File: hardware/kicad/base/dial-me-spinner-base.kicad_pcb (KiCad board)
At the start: 2 copper layers, 57.6 x 46 mm, 23 parts, among them J1 TYPE-C-31-M-12, J2 BATT, J3 LINK, Q1 BSS138DW, SW1 TS-1187A, U1 BQ25180YBGR, U2 USBLC6-2SC6

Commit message: WIP: firmware/bring-up docs review fixes; routing in progress
Co-Authored-By: Claude Opus 5.5 <noreply@anthropic.com>
Claude-Session: https://claude.ai/code/session_01P3cqdBhxLcWY3sGUVf9LAJ
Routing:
- net GND: track 0.00 -> 175.6 mm
- net VBUS: track 0.00 -> 81.7 mm, vias 0 -> 4
- net /Base board/USB_DM: track 6.35 -> 58.4 mm, vias 0 -> 4
- net /Base board/USB_DP: track 4.35 -> 53.6 mm, vias 2 -> 4
- net VBAT: track 0.00 -> 43.5 mm, vias 0 -> 4
- net /Base board/I2C_SCL: track 0.00 -> 42.1 mm, vias 0 -> 2
- net /Base board/I2C_SDA: track 0.00 -> 35.3 mm, vias 0 -> 2
- net /Base board/BTN_N: track 0.00 -> 30.3 mm, vias 0 -> 2
- net /Base board/CHG_TSMR: track 0.00 -> 23.3 mm
- net /Base board/CHG_INT_N: track 0.00 -> 15.0 mm, vias 0 -> 1
- net /Base board/SW_GATE: track 0.00 -> 9.14 mm
- net VSYS: track 0.00 -> 8.18 mm
- net /Base board/SW_HI: track 0.00 -> 7.97 mm
- net /Base board/USB_CC1: track 0.00 -> 4.07 mm
- net /Base board/USB_CC2: track 0.00 -> 2.43 mm

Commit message: WIP: BGA escape pre-route for the charger; routing in progress
Co-Authored-By: Claude Opus 5.5 <noreply@anthropic.com>
Claude-Session: https://claude.ai/code/session_01P3cqdBhxLcWY3sGUVf9LAJ
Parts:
- moved C2 4.99 mm to (113.1, 105.8)
- moved TP2 4.29 mm to (107.6, 106.6)
- moved C1 3.08 mm to (110.2, 103.4), turned to 0 degrees
- moved C3 0.40 mm to (111.5, 108.5)
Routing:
- net /Base board/CHG_INT_N: track 15.0 -> 45.2 mm, vias 1 -> 2
- net GND: track 175.6 -> 147.9 mm
- net VBUS: track 81.7 -> 59.4 mm, vias 4 -> 0
- net /Base board/CHG_TSMR: track 23.3 -> 39.2 mm
- net VBAT: track 43.5 -> 54.4 mm, vias 4 -> 3
- net /Base board/SW_GATE: track 9.14 -> 19.4 mm, vias 0 -> 2
- net /Base board/I2C_SCL: track 42.1 -> 47.3 mm
- net /Base board/I2C_SDA: track 35.3 -> 36.5 mm
- net /Base board/USB_CC1: track 4.07 -> 5.19 mm, vias 0 -> 2
- net /Base board/USB_DM: track 58.4 -> 59.3 mm
- net VSYS: track 8.18 -> 7.38 mm
- net /Base board/USB_DP: track 53.6 -> 53.0 mm

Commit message: WIP: VSYS escape via on the charger BGA
Co-Authored-By: Claude Opus 5.5 <noreply@anthropic.com>
Claude-Session: https://claude.ai/code/session_01P3cqdBhxLcWY3sGUVf9LAJ
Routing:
- net /Base board/I2C_SCL: track 47.3 -> 41.3 mm
- net VBAT: track 54.4 -> 49.8 mm
- net /Base board/USB_DP: track 53.0 -> 51.4 mm
- net /Base board/CHG_INT_N: track 45.2 -> 44.2 mm
- net /Base board/USB_CC1: track 5.19 -> 4.44 mm
- net /Base board/USB_CC2: track 2.43 -> 3.08 mm
- net VBUS: track 59.4 -> 60.1 mm
- net /Base board/USB_DM: track 59.3 -> 58.7 mm

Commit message: Apply schematic review fixes; base board routes to 100% with zero DRC errors
- OLED VCC input disconnect is now a TPS22917 load switch (CT to VIN) instead
  of an AO3401A/2N7002 with no real inrush control
- TPD4E05U06 TVS on the TMAG5273 lines (floating 316L ring passes 2.4 mm away)
- piezo: 470R series + 1M bleed; LED_DIN pull-down moved to the shifter input
- base: explicit 2x4 DSBGA fan-out for the BQ25180, 0.4 mm power tracks,
  BAT+/GND silkscreen at the battery connector, JEITA NTC over the pack
- SPEC: side-entry link headers on both boards, 28 AWG power leads

Co-Authored-By: Claude Opus 5.5 <noreply@anthropic.com>
Claude-Session: https://claude.ai/code/session_01P3cqdBhxLcWY3sGUVf9LAJ
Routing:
- net VSYS: track 7.38 -> 39.0 mm, vias 0 -> 2
- net /Base board/CHG_INT_N: track 44.2 -> 32.3 mm, vias 2 -> 0
- net VBAT: track 49.8 -> 39.0 mm, vias 3 -> 2
- net /Base board/I2C_SCL: track 41.3 -> 30.6 mm, vias 2 -> 0
- net GND: track 148.0 -> 155.3 mm, vias 0 -> 4
- net /Base board/USB_DM: track 58.7 -> 52.8 mm, vias 4 -> 3
- net /Base board/SW_GATE: track 19.4 -> 13.7 mm, vias 2 -> 0
- net VBUS: track 60.1 -> 64.9 mm, vias 0 -> 2
- net /Base board/CHG_TSMR: track 39.3 -> 35.3 mm, vias 0 -> 3
- net /Base board/BTN_N: track 30.1 -> 27.8 mm
- net /Base board/I2C_SDA: track 36.5 -> 38.4 mm
- net /Base board/USB_DP: track 51.4 -> 50.7 mm
- net /Base board/USB_CC1: track 4.44 -> 5.09 mm
- net /Base board/USB_CC2: track 3.08 -> 2.43 mm
- added copper zone on B.Cu, net GND
- added copper zone on F.Cu, net GND

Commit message: WIP: re-placed boards (routing in progress)
Co-Authored-By: Claude Opus 5.5 <noreply@anthropic.com>
Claude-Session: https://claude.ai/code/session_01P3cqdBhxLcWY3sGUVf9LAJ
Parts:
- RT1: moved to B.Cu
- moved RT1 16.5 mm to (92.5, 102.7)
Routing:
- net GND: track 155.3 -> 0.95 mm, vias 4 -> 1
- net VBUS: track 64.9 -> 0.80 mm, vias 2 -> 0
- net /Base board/USB_DM: track 52.8 -> 6.35 mm, vias 3 -> 0
- net /Base board/USB_DP: track 50.7 -> 4.35 mm, vias 4 -> 2
- net VBAT: track 39.0 -> 1.34 mm, vias 2 -> 0
- net VSYS: track 39.0 -> 1.40 mm, vias 2 -> 0
- net /Base board/I2C_SDA: track 38.4 -> 0.80 mm, vias 2 -> 0
- net /Base board/CHG_TSMR: track 35.3 -> 0.80 mm, vias 3 -> 0
- net /Base board/CHG_INT_N: track 32.3 -> 0.80 mm
- net /Base board/I2C_SCL: track 30.6 -> 0.80 mm
- net /Base board/BTN_N: track 27.8 -> 0.00 mm, vias 2 -> 0
- net /Base board/SW_GATE: track 13.7 -> 0.00 mm
- net /Base board/SW_HI: track 8.30 -> 0.00 mm
- net /Base board/USB_CC1: track 5.09 -> 0.00 mm, vias 2 -> 0
- net /Base board/USB_CC2: track 2.43 -> 0.00 mm
- removed copper zone on B.Cu, net GND
- removed copper zone on F.Cu, net GND
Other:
- board text added: "BAT+"
- board text added: "GND"

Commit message: WIP: base board rerouted
Co-Authored-By: Claude Opus 5.5 <noreply@anthropic.com>
Claude-Session: https://claude.ai/code/session_01P3cqdBhxLcWY3sGUVf9LAJ
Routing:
- net GND: track 0.95 -> 151.5 mm, vias 1 -> 3
- net VBUS: track 0.80 -> 75.8 mm, vias 0 -> 3
- net /Base board/USB_DM: track 6.35 -> 73.6 mm, vias 0 -> 3
- net /Base board/I2C_SDA: track 0.80 -> 60.7 mm, vias 0 -> 4
- net /Base board/USB_DP: track 4.35 -> 57.7 mm, vias 2 -> 4
- net VBAT: track 1.34 -> 46.1 mm
- net /Base board/CHG_INT_N: track 0.80 -> 42.7 mm, vias 0 -> 2
- net /Base board/BTN_N: track 0.00 -> 40.9 mm, vias 0 -> 2
- net /Base board/I2C_SCL: track 0.80 -> 37.2 mm, vias 0 -> 2
- net VSYS: track 1.40 -> 36.0 mm, vias 0 -> 2
- net /Base board/CHG_TSMR: track 0.80 -> 23.0 mm, vias 0 -> 2
- net /Base board/SW_GATE: track 0.00 -> 13.2 mm
- net /Base board/USB_CC1: track 0.00 -> 9.80 mm
- net /Base board/SW_HI: track 0.00 -> 7.85 mm
- net /Base board/USB_CC2: track 0.00 -> 5.09 mm, vias 0 -> 2
- added copper zone on B.Cu, net GND
- added copper zone on F.Cu, net GND

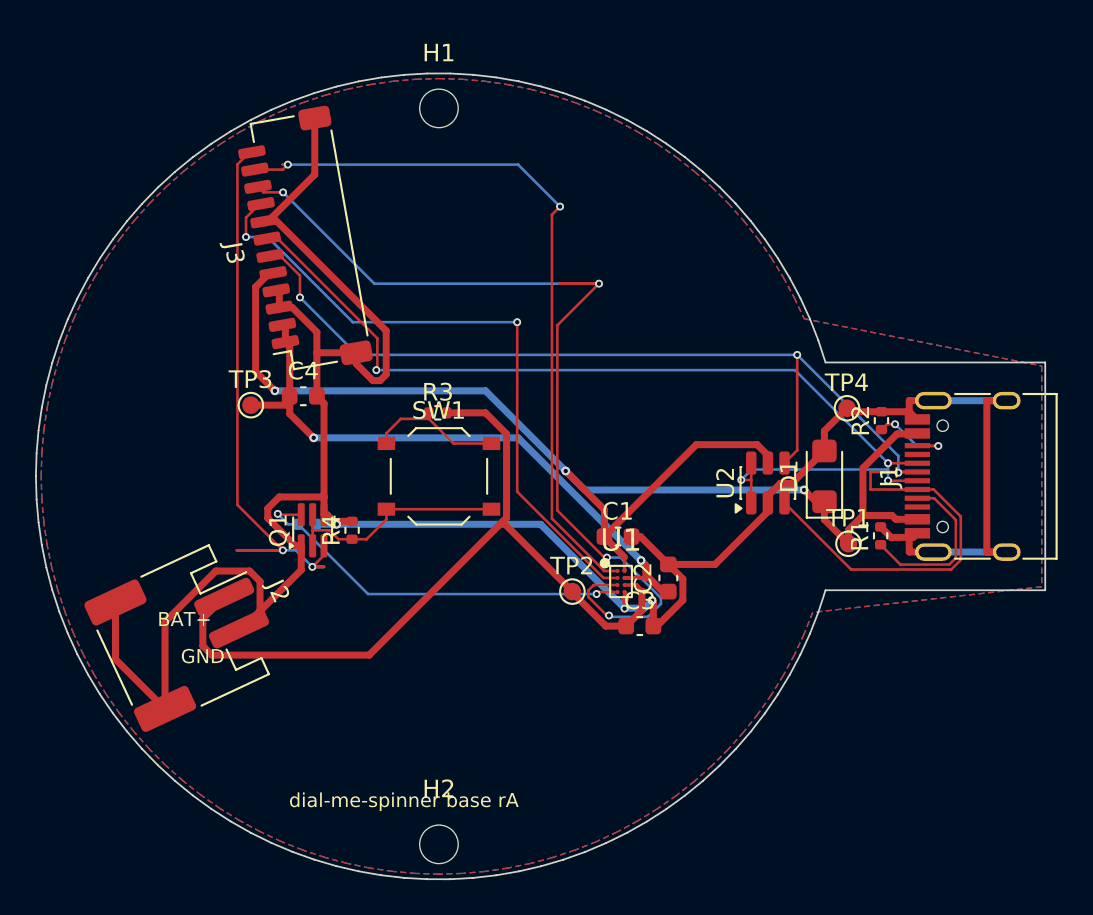
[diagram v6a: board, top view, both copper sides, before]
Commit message: WIP: re-placed boards with fiducials (routing in progress), --finish clean-up step
Co-Authored-By: Claude Opus 5.5 <noreply@anthropic.com>
Claude-Session: https://claude.ai/code/session_01P3cqdBhxLcWY3sGUVf9LAJ
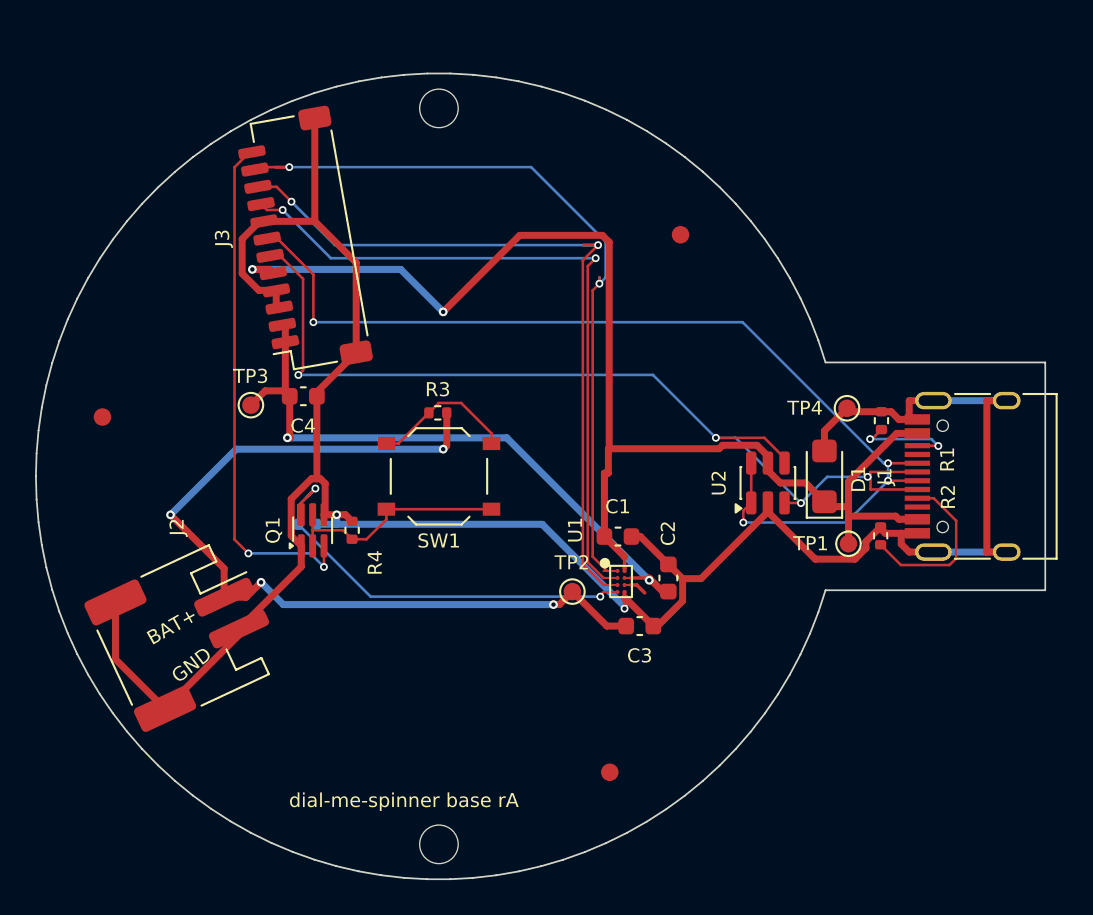
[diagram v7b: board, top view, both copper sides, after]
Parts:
- added FID1: Fiducial_1mm_Mask2mm, Fiducial:Fiducial_1mm_Mask2mm, F.Cu at (113.8, 86.2)
- added FID2: Fiducial_1mm_Mask2mm, Fiducial:Fiducial_1mm_Mask2mm, F.Cu at (80.8, 96.6)
- added FID3: Fiducial_1mm_Mask2mm, Fiducial:Fiducial_1mm_Mask2mm, F.Cu at (109.8, 116.9)
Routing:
- net /Base board/USB_DM: track 73.6 -> 56.3 mm, vias 3 -> 4
- net /Base board/I2C_SDA: track 60.7 -> 43.5 mm, vias 4 -> 2
- net /Base board/BTN_N: track 40.9 -> 29.5 mm
- net GND: track 151.5 -> 142.0 mm, vias 3 -> 2
- net VBAT: track 46.1 -> 51.5 mm, vias 0 -> 4
- net VBUS: track 75.8 -> 72.6 mm, vias 3 -> 2
- net /Base board/I2C_SCL: track 37.2 -> 40.3 mm
- net /Base board/CHG_TSMR: track 23.0 -> 25.7 mm
- net /Base board/USB_DP: track 57.7 -> 59.5 mm
- net /Base board/CHG_INT_N: track 42.7 -> 44.4 mm
- net /Base board/USB_CC2: track 5.09 -> 6.26 mm
- removed copper zone on B.Cu, net GND
- removed copper zone on F.Cu, net GND

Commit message: Fix footprint orientation fit (duplicate MP pads), base-board review fixes in progress
- layout.local_map pairs pads by list position, so J1/J3/J2 now face the right way
- base: J2 at θ 222° mouth outward, RT1 on top, BQ25180 off the pack at θ 255°,
  Q1 out of the spoke sector, one boss at r 20 + rib, antenna copper keep-outs
- finish step: zone-aware debris removal, DRC-driven dangling prune, GND stitching
- drc() reports warnings and schematic parity

Co-Authored-By: Claude Opus 5.5 <noreply@anthropic.com>
Claude-Session: https://claude.ai/code/session_01P3cqdBhxLcWY3sGUVf9LAJ
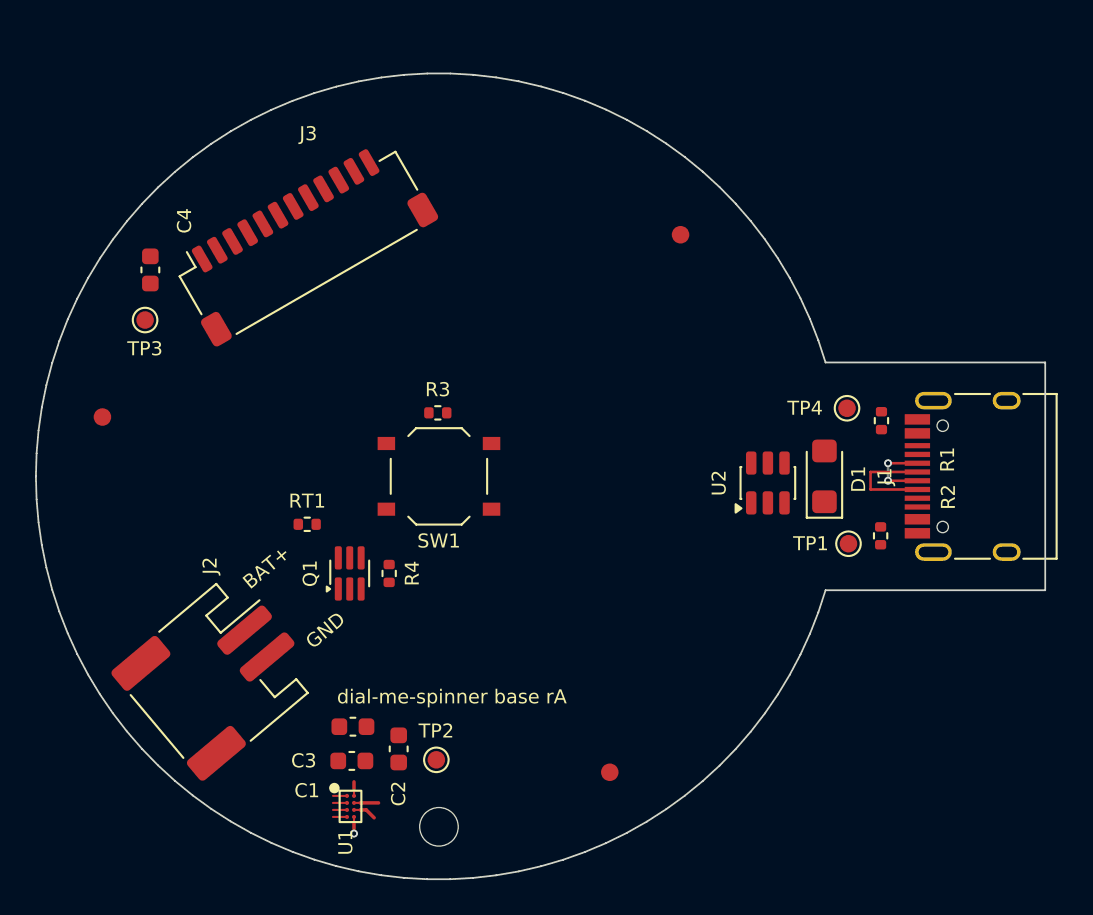
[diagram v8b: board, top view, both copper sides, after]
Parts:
- removed H2: MountingHole_2.2mm_M2, MountingHole:MountingHole_2.2mm_M2
- RT1: moved to F.Cu
- moved H1 41.0 mm to (100.0, 120.0)
- moved U1 20.1 mm to (95.0, 118.8)
- moved C1 19.9 mm to (95.0, 116.2)
- moved C2 18.2 mm to (97.7, 115.6)
- moved C3 17.3 mm to (95.1, 114.3)
- moved TP2 12.3 mm to (99.9, 116.2)
- moved C4 11.3 mm to (83.5, 88.2), turned to 90 degrees
- moved TP3 7.75 mm to (83.2, 91.1)
- moved Q1 3.25 mm to (94.9, 105.5)
- moved R4 3.25 mm to (97.2, 105.5)
- moved J2 2.96 mm to (87.4, 111.4), turned to -50 degrees
- turned J3 to 30 degrees
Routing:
- net GND: track 142.0 -> 0.95 mm, vias 2 -> 1
- net VBUS: track 72.6 -> 0.80 mm, vias 2 -> 0
- net /Base board/USB_DP: track 59.5 -> 4.35 mm, vias 4 -> 2
- net VBAT: track 51.5 -> 1.34 mm, vias 4 -> 0
- net /Base board/USB_DM: track 56.3 -> 6.35 mm, vias 4 -> 0
- net /Base board/CHG_INT_N: track 44.4 -> 0.80 mm, vias 2 -> 0
- net /Base board/I2C_SDA: track 43.5 -> 0.80 mm, vias 2 -> 0
- net /Base board/I2C_SCL: track 40.3 -> 0.80 mm, vias 2 -> 0
- net VSYS: track 36.3 -> 1.40 mm, vias 2 -> 0
- net /Base board/BTN_N: track 29.5 -> 0.00 mm, vias 2 -> 0
- net /Base board/CHG_TSMR: track 25.7 -> 0.80 mm, vias 2 -> 0
- net /Base board/SW_GATE: track 13.2 -> 0.00 mm
- net /Base board/USB_CC1: track 9.84 -> 0.00 mm
- net /Base board/SW_HI: track 8.27 -> 0.00 mm
- net /Base board/USB_CC2: track 6.26 -> 0.00 mm, vias 2 -> 0
